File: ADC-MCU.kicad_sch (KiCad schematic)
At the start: 0 parts

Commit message: ADC-MCU and power latch
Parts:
- added C1: 0.1u, Capacitor_SMD:C_1812_4532Metric, symbol Device:C
- added C11, C16: 1u, Capacitor_SMD:C_0805_2012Metric, symbol Device:C
- added C12: 0.1u, Capacitor_SMD:C_0805_2012Metric, symbol Device:C
- added C13: 10u, Capacitor_SMD:C_0805_2012Metric, symbol Device:C
- added C2: C, symbol Device:C
- added D1, D2: SS14, Diode_SMD:D_SMA, symbol Diode:SS14
- added J1: 2171790001, 2171790001:MOLEX_2171790001, symbol 2171790001:2171790001
- added R1: 180k, Resistor_SMD:R_0805_2012Metric, symbol Device:R
- added R10, R9: 5.1k, Resistor_SMD:R_0805_2012Metric, symbol Device:R
- added R2, R3, R4, R5: R, symbol Device:R
- added R24: 10k, Resistor_SMD:R_0805_2012Metric, symbol Device:R
- added R6, R7, R8: 0, Resistor_SMD:R_0805_2012Metric, symbol Device:R
- added SW1, SW2: SW_Push, Button_Switch_THT:SW_PUSH_6mm, symbol Switch:SW_Push
- added TP5, TP6, TP7, TP8: TestPoint, Connector_Pin:Pin_D1.0mm_L10.0mm, symbol Connector:TestPoint
- added U1: OPA2140AIDR, D8, symbol OPA2140AIDR:OPA2140AIDR
- added U2: CD4052BPWR, PW0016A_N, symbol CD4052BPWR:CD4052BPWR
- added U3: LM393DR, LM393DR:SOIC127P599X175-8N, symbol LM393DR:LM393DR
- added U4: ADG601BRMZ-REEL7, ADG601BRMZ-REEL7:SOP65P490X110-8N, symbol ADG601BRMZ-REEL7:ADG601BRMZ-REEL7
- added U5: ESP32-C3-WROOM-02-N4, ESP32-C3-WROOM-02-N4:MODULE_ESP32-C3-WROOM-02-H4, symbol ESP32-C3-WROOM-02-N4:ESP32-C3-WROOM-02-N4
- added U6: AP2112K-3.3, Package_TO_SOT_SMD:SOT-23-5, symbol Regulator_Linear:AP2112K-3.3
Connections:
- new net: C1.1, R1.2, U1.2 (INA-), U4.8 (S)
- new net: C1.2, TP5.1, U1.1 (OUTA), U3.3 (1IN+), U3.6 (2IN-), U4.1 (D)
- new net: C2.2, D1.1 (K), D2.1 (K), U6.1 (VIN), U6.3 (EN)
- new net: J1.B5 (CC2), R9.2
- new net: R1.1, U2.13 (X_COM_I_O)
- new net: J1.A5 (CC1), R10.2
- new net: R2.1, R3.2, U1.6 (INB-)
- new net: C11.2, R24.1, U5.2 (EN)
- new net +3V3: C16.2, R4.2, R5.2, U1.8 (V+), U2.1 (Y_CH_I_O_0), U2.16 (VDD), U3.8 (VCC), U4.4 (VDD), U6.5 (VOUT)
- new net +5V: D1.2 (A), J1.A4B9 (VBUS1), J1.B4A9 (VBUS2)
- new net +9V: D2.2 (A)
- new net -VREF: R3.1, TP8.1, U1.7 (OUTB), U2.11 (X_CH_I_O_3)
- new net 1.65V: U1.3 (INA+), U2.12 (X_CH_I_O_0), U3.2 (1IN-), U3.5 (2IN+)
- new net 3V3: C12.2, C13.2, R24.2, U5.1 (3V3)
- new net ADC_IN1: R6.1, R7.1
- new net ADC_IN2: R8.1
- new net BOOT: SW1.1, U5.8 (IO9)
- new net COMP_OUT: R4.1, TP7.1, U3.1 (1OUT), U5.10 (IO10)
- new net COMP_OUT_BAR: R5.1, TP6.1, U3.7 (2OUT), U5.12 (TXD)
- new net DS_ADC: R6.2, U2.15 (X_CH_I_O_2)
- new net EN: SW2.2
- new net ESP_ADC_1: R7.2, U5.18 (IO0)
- new net ESP_ADC_2: R8.2, U5.17 (IO1)
- new net GND: C11.1, C12.1, C13.1, C16.1, C2.1, J1.A1B12 (GND1), J1.B1A12 (GND2), J1.SH1 (SHIELD1), J1.SH2 (SHIELD2), J1.SH3 (SHIELD3), J1.SH4 (SHIELD4), R10.1, R9.1, SW1.2, SW2.1, U1.4 (V-), U1.5 (INB+), U2.2 (Y_CH_I_O_2), U2.4 (Y_CH_I_O_3), U2.5 (Y_CH_I_O_1), U2.6 (INH), U2.7 (VEE), U2.8 (VSS), U3.4 (GND), U4.5 (VSS), U4.7 (GND), U5.19 (GND), U5.20 (GND), U5.21 (GND), U5.22 (GND), U5.23 (GND), U5.24 (GND), U5.25 (GND), U5.26 (GND), U5.27 (GND), U5.28 (GND), U5.29 (GND), U5.30 (GND), U5.31 (GND), U5.32 (GND), U5.33 (GND), U5.34 (GND), U5.35 (GND), U5.36 (GND), U5.37 (GND), U5.38 (GND), U5.39 (GND), U5.9 (GND), U6.2 (GND)
- new net MUX_A: U2.10 (A), U5.6 (IO7)
- new net MUX_B: U2.9 (B), U5.11 (RXD)
- new net POWER_LATCH: U5.15 (IO3)
- new net RST_SW: U2.3 (Y_COM_I_O), U4.6 (IN), U5.3 (IO4)
- new net SCL: U5.4 (IO5)
- new net SDA: U5.5 (IO6)
- new net USB_D+: J1.A6 (DP1), J1.B6 (DP2), U5.14 (IO19)
- new net USB_D-: J1.A7 (DN1), J1.B7 (DN2), U5.13 (IO18)
- new net V_BG: R2.2, U2.14 (X_CH_I_O_1)
- no-connect marks 0 -> 4

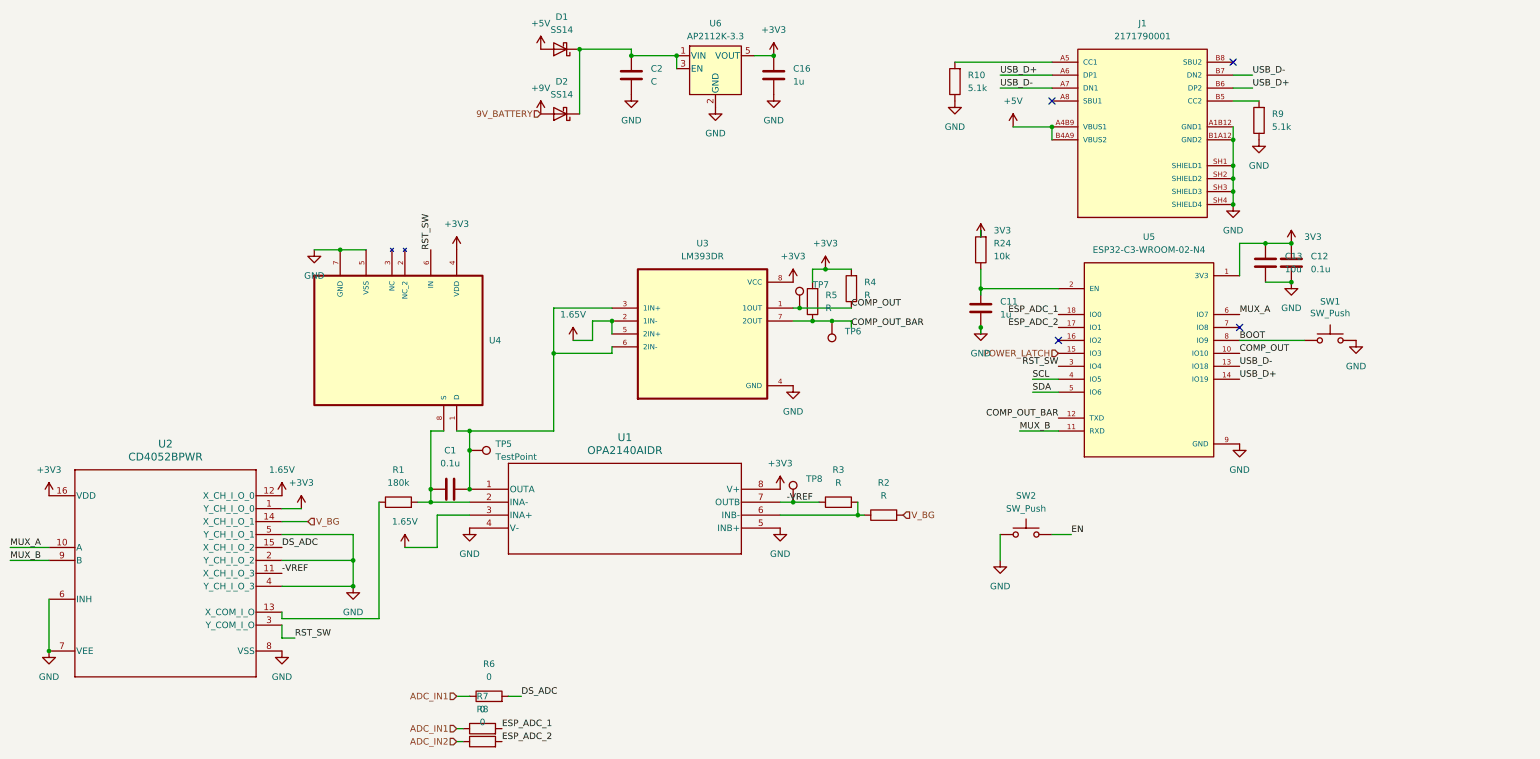
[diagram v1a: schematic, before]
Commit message: added 1.65v reference and decoupling caps
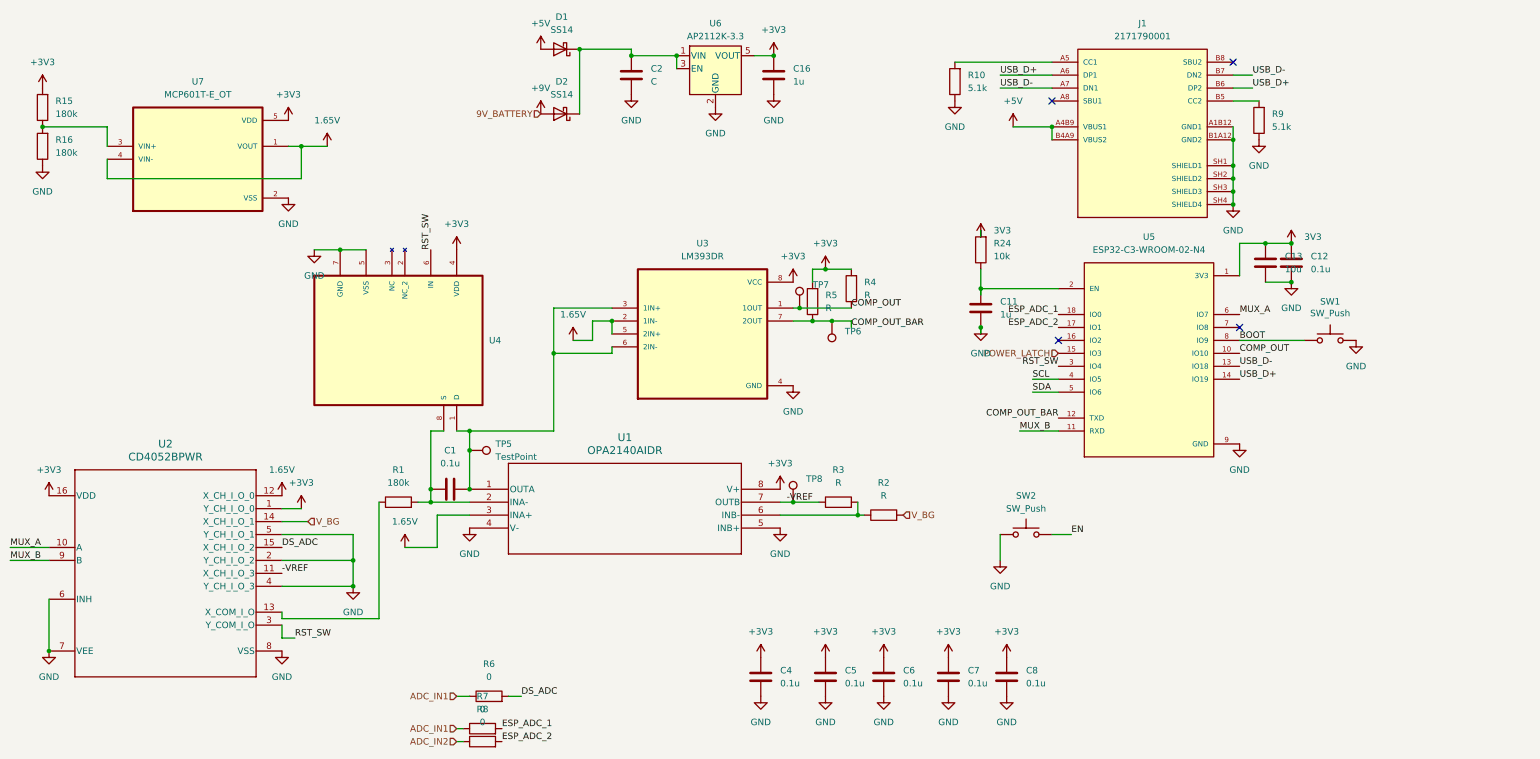
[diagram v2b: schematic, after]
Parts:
- added C4, C5, C6, C7, C8: 0.1u, Capacitor_SMD:C_0805_2012Metric, symbol Device:C
- added R15, R16: 180k, Resistor_SMD:R_0805_2012Metric, symbol Device:R
- added U7: MCP601T-E_OT, MCP601T-E_OT:SOT95P270X145-5N, symbol MCP601T-E_OT:MCP601T-E_OT
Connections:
- net +3V3: now also C4.2, C5.2, C6.2, C7.2, C8.2, R15.2, U7.5 (VDD)
- net 1.65V: now also U7.1 (VOUT), U7.4 (VIN-)
- net GND: now also C4.1, C5.1, C6.1, C7.1, C8.1, R16.1, U7.2 (VSS)
- new net: R15.1, R16.2, U7.3 (VIN+)

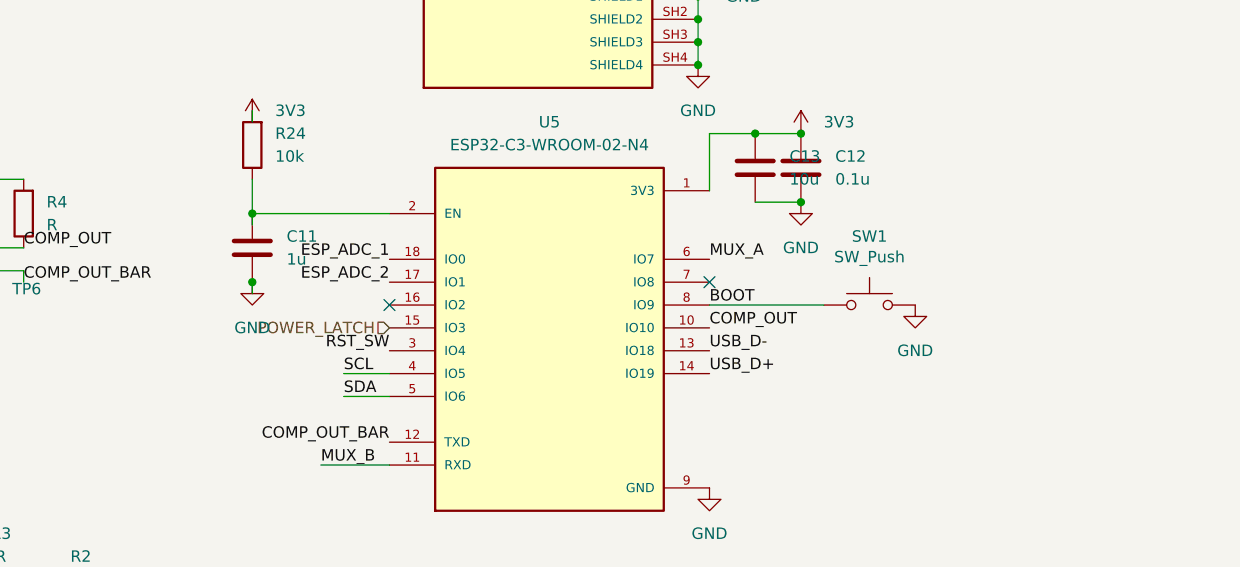
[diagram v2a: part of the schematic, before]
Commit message: added pullup resistors
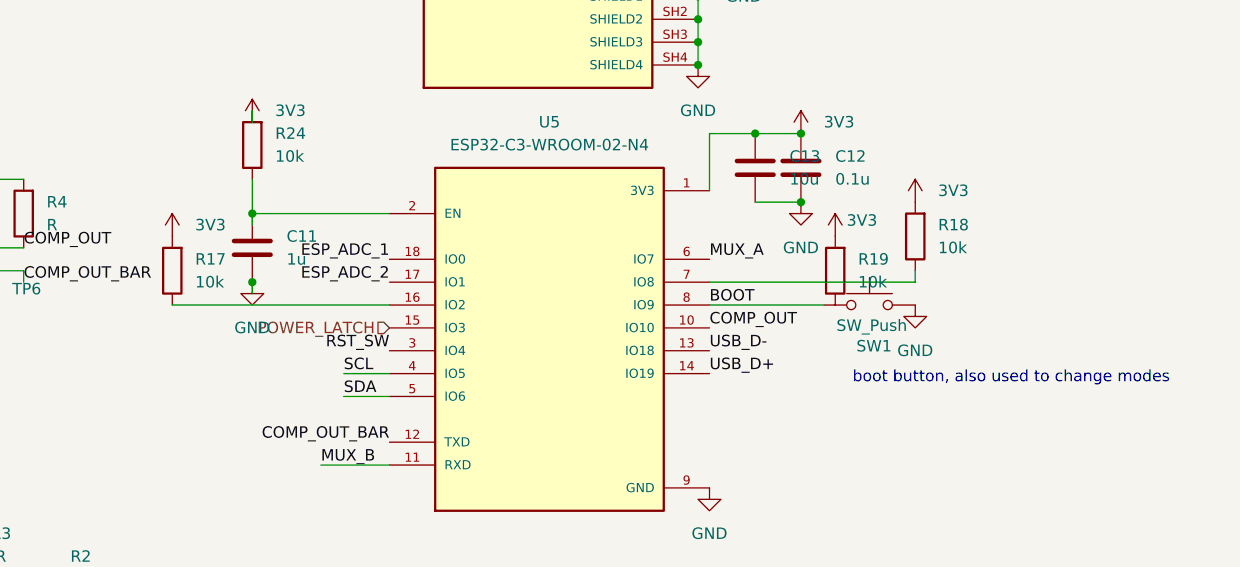
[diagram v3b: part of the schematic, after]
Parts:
- added R17, R18, R19: 10k, Resistor_SMD:R_0805_2012Metric, symbol Device:R
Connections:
- net 3V3: now also R17.2, R18.2, R19.2
- net at U5.16 (IO2): now also R17.1
- net at U5.7 (IO8): now also R18.1
- no-connect marks 4 -> 2
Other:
- note added: "boot button, also used to change modes"

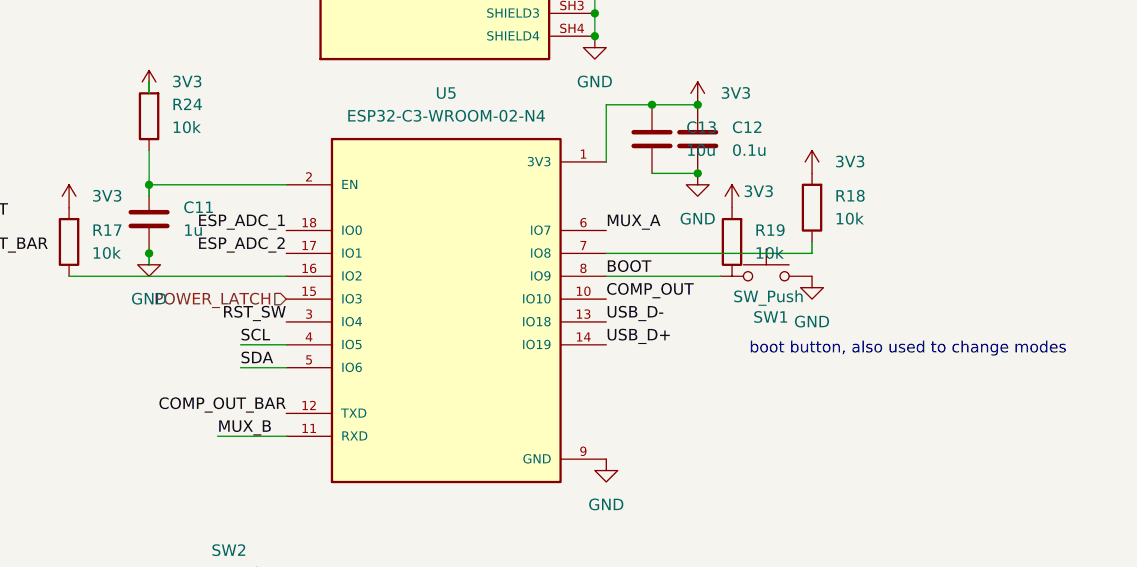
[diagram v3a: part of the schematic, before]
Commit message: added range sel
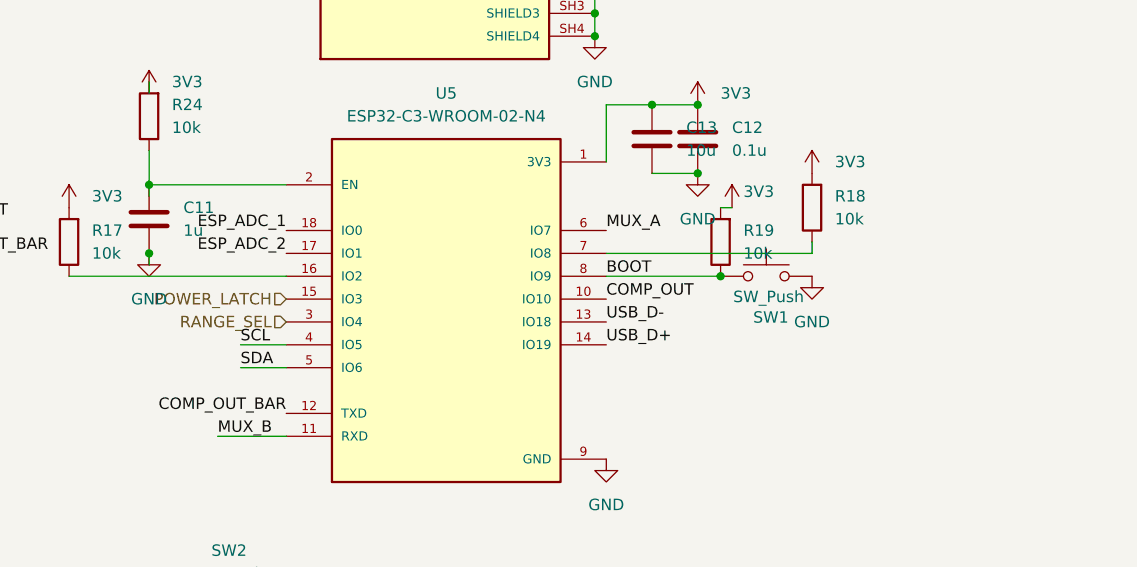
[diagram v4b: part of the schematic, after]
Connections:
- net BOOT: now also R19.1
- net RST_SW: no longer U5.3 (IO4)
- new net RANGE_SEL: U5.3 (IO4)
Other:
- note removed: "boot button, also used to change modes"
- moved on the sheet: R19
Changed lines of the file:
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@@
 	(generator_version "9.0")
 	(paper "A4")
-	(text "boot button, also used to change modes"
-		(exclude_from_sim no)
-		(at 290.068 85.598 0)
-		(effects
-			(font
-				(size 1.27 1.27)
-			)
-		)
-	)
 	(junction
 		(at 105.41 99.06)
@@
 	(junction
 		(at 255.27 38.1)
+		(diameter 0)
+		(color 0 0 0 0)
+	)
+	(junction
+		(at 269.24 77.47)
 		(diameter 0)
 		(color 0 0 0 0)
@@
 	(wire
 		(pts
+			(xy 269.24 69.85) (xy 270.51 69.85)
+		)
+		(stroke
+			(width 0)
+			(type default)
+		)
+	)
+	(wire
+		(pts
 			(xy 256.54 58.42) (xy 256.54 64.77)
 		)
@@
 			)
 			(justify left bottom)
-		)
-	)
-	(label "RST_SW"
-		(at 220.98 82.55 180)
-		(effects
-			(font
-				(size 1.27 1.27)
-			)
-			(justify right bottom)
 		)
 	)
@@
 			)
 			(justify left)
+		)
+	)
+	(hierarchical_label "RANGE_SEL"
+		(shape input)
+		(at 220.98 82.55 180)
+		(effects
+			(font
+				(size 1.27 1.27)
+			)
+			(justify right)
 		)
 	)
@@
 	(symbol
 		(lib_id "Device:R")
-		(at 270.51 73.66 180)
+		(at 269.24 73.66 180)
 		(unit 1)
 		(exclude_from_sim no)
@@
 		(fields_autoplaced yes)
 		(property "Reference" "R19"
-			(at 273.05 72.3899 0)
+			(at 271.78 72.3899 0)
 			(effects
 				(font
@@
 		)
 		(property "Value" "10k"
-			(at 273.05 74.9299 0)
+			(at 271.78 74.9299 0)
 			(effects
 				(font
@@
 		)
 		(property "Footprint" "Resistor_SMD:R_0805_2012Metric"
-			(at 272.288 73.66 90)
+			(at 271.018 73.66 90)
 			(effects
 				(font
@@
 		)
 		(property "Datasheet" "~"
-			(at 270.51 73.66 0)
+			(at 269.24 73.66 0)
 			(effects
 				(font
@@
 		)
 		(property "Description" "Resistor"
-			(at 270.51 73.66 0)
-			(effects
-				(font
+			(at 269.24 73.66 0)
+			(effects
+				(font

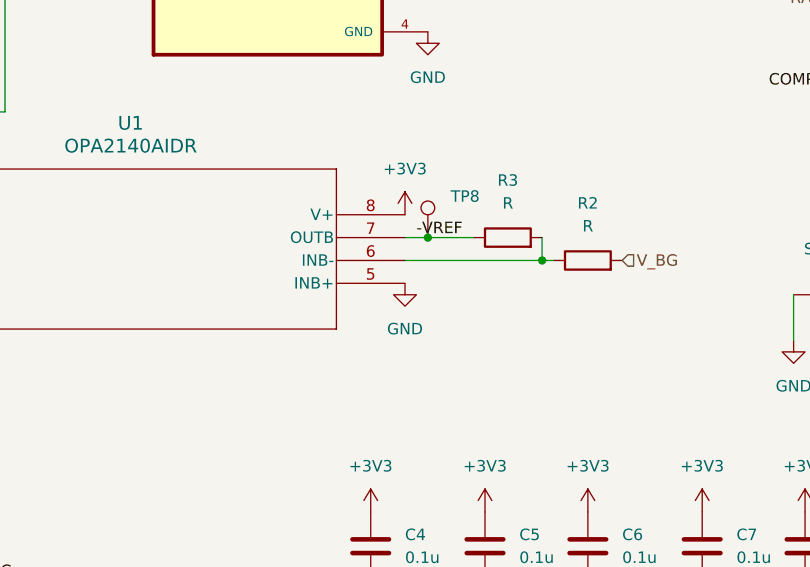
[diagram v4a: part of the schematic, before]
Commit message: added footprints
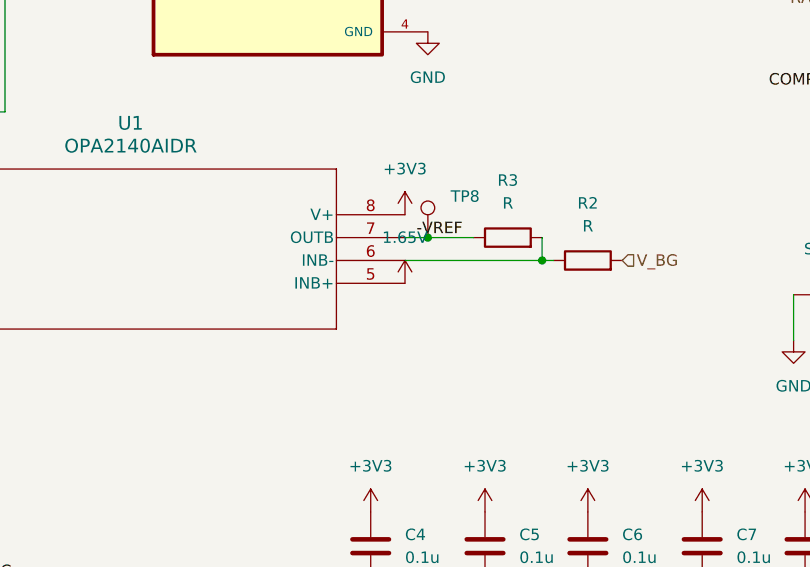
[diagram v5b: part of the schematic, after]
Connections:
- net 1.65V: now also U1.5 (INB+)
- net GND: no longer U1.5 (INB+)
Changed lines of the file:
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@@
+	)
+	(symbol
+		(lib_id "power:+3V3")
+		(at 166.37 114.3 0)
+		(unit 1)
+		(exclude_from_sim no)
+		(in_bom yes)
+		(on_board yes)
+		(dnp no)
+		(fields_autoplaced yes)
+		(property "Reference" "#PWR05"
+			(at 166.37 118.11 0)
+			(effects
+				(font
+					(size 1.27 1.27)
+				)
+				(hide yes)
+			)
+		)
+		(property "Value" "1.65V"
+			(at 166.37 109.22 0)
+			(effects
+				(font
+					(size 1.27 1.27)
+				)
+			)
+		)
+		(property "Footprint" ""
+			(at 166.37 114.3 0)
+			(effects
+				(font
+					(size 1.27 1.27)
+				)
+				(hide yes)
+			)
+		)
+		(property "Datasheet" ""
+			(at 166.37 114.3 0)
+			(effects
+				(font
+					(size 1.27 1.27)
+				)
+				(hide yes)
+			)
+		)
+		(property "Description" "Power symbol creates a global label with name \"+3V3\""
+			(at 166.37 114.3 0)
+			(effects
+				(font
+					(size 1.27 1.27)
+				)
+				(hide yes)
+			)
+		)
+		(pin "1"
+		)
+		(instances
+			(project "ee115-capstone"
+				(path "/80dfed98-7d85-4c9a-bb85-182165e7352f/70c590be-37b3-451b-9092-80cd15b0f8be"
+					(reference "#PWR05")
+					(unit 1)
+				)
+			)
+		)
 	)
 	(symbol
@@
 					(unit 1)
 				)
-			)
-		)
-	)
-	(symbol
-		(lib_id "power:GND")
-		(at 166.37 114.3 0)
-		(unit 1)
-		(exclude_from_sim no)
-		(in_bom yes)
-		(on_board yes)
-		(dnp no)
-		(fields_autoplaced yes)
-		(property "Reference" "#PWR05"
-			(at 166.37 120.65 0)
-			(effects
-				(font
-					(size 1.27 1.27)
-				)
-				(hide yes)
-			)
-		)
-		(property "Value" "GND"
-			(at 166.37 119.38 0)
-			(effects
-				(font
-					(size 1.27 1.27)
-				)
-			)
-		)
-		(property "Footprint" ""
-			(at 166.37 114.3 0)
-			(effects
-				(font
-					(size 1.27 1.27)
-				)
-				(hide yes)
-			)
-		)
-		(property "Datasheet" ""
-			(at 166.37 114.3 0)
-			(effects
-				(font
-					(size 1.27 1.27)
-				)
-				(hide yes)
-			)
-		)
-		(property "Description" "Power symbol creates a global label with name \"GND\" , ground"
-			(at 166.37 114.3 0)
-			(effects
-				(font
-					(size 1.27 1.27)
-				)
-				(hide yes)
-			)
-		)
-		(pin "1"
-		)
-		(instances
-			(project "ee115-capstone"
-				(path "/80dfed98-7d85-4c9a-bb85-182165e7352f/70c590be-37b3-451b-9092-80cd15b0f8be"
-					(reference "#PWR05")
-					(unit 1)
-				)
